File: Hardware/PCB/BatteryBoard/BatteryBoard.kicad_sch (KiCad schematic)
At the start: 59 parts, among them J1 Conn_01x07, J2 USB_C_Receptacle_USB2.0, J3 Conn_01x07, J4 Conn_01x07, J5 Thermistor, J6 Conn_01x07, J7 Power, Q1 FDS4935A, Q2 BCV62, SW1 SW_SPDT, U1 BQ25887RGER, U2 NJW4190M, U3 AZ1084C-3.3, U4 MIC29500-5.0WT

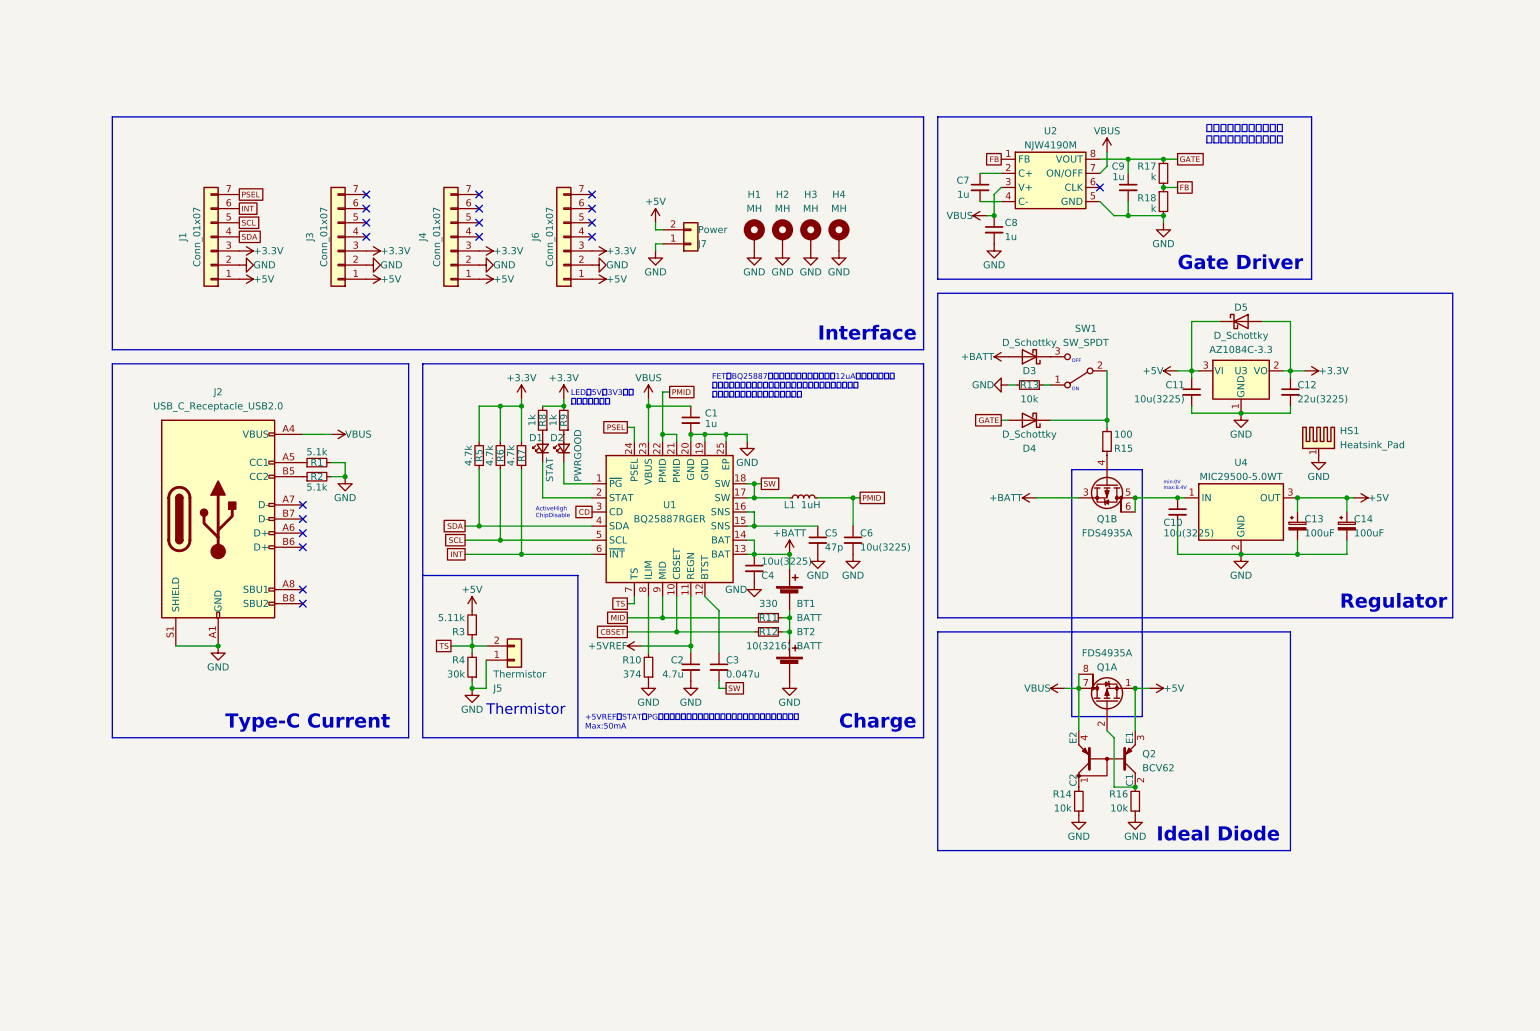
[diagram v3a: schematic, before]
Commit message: Powerpathコンを使用、部品配置
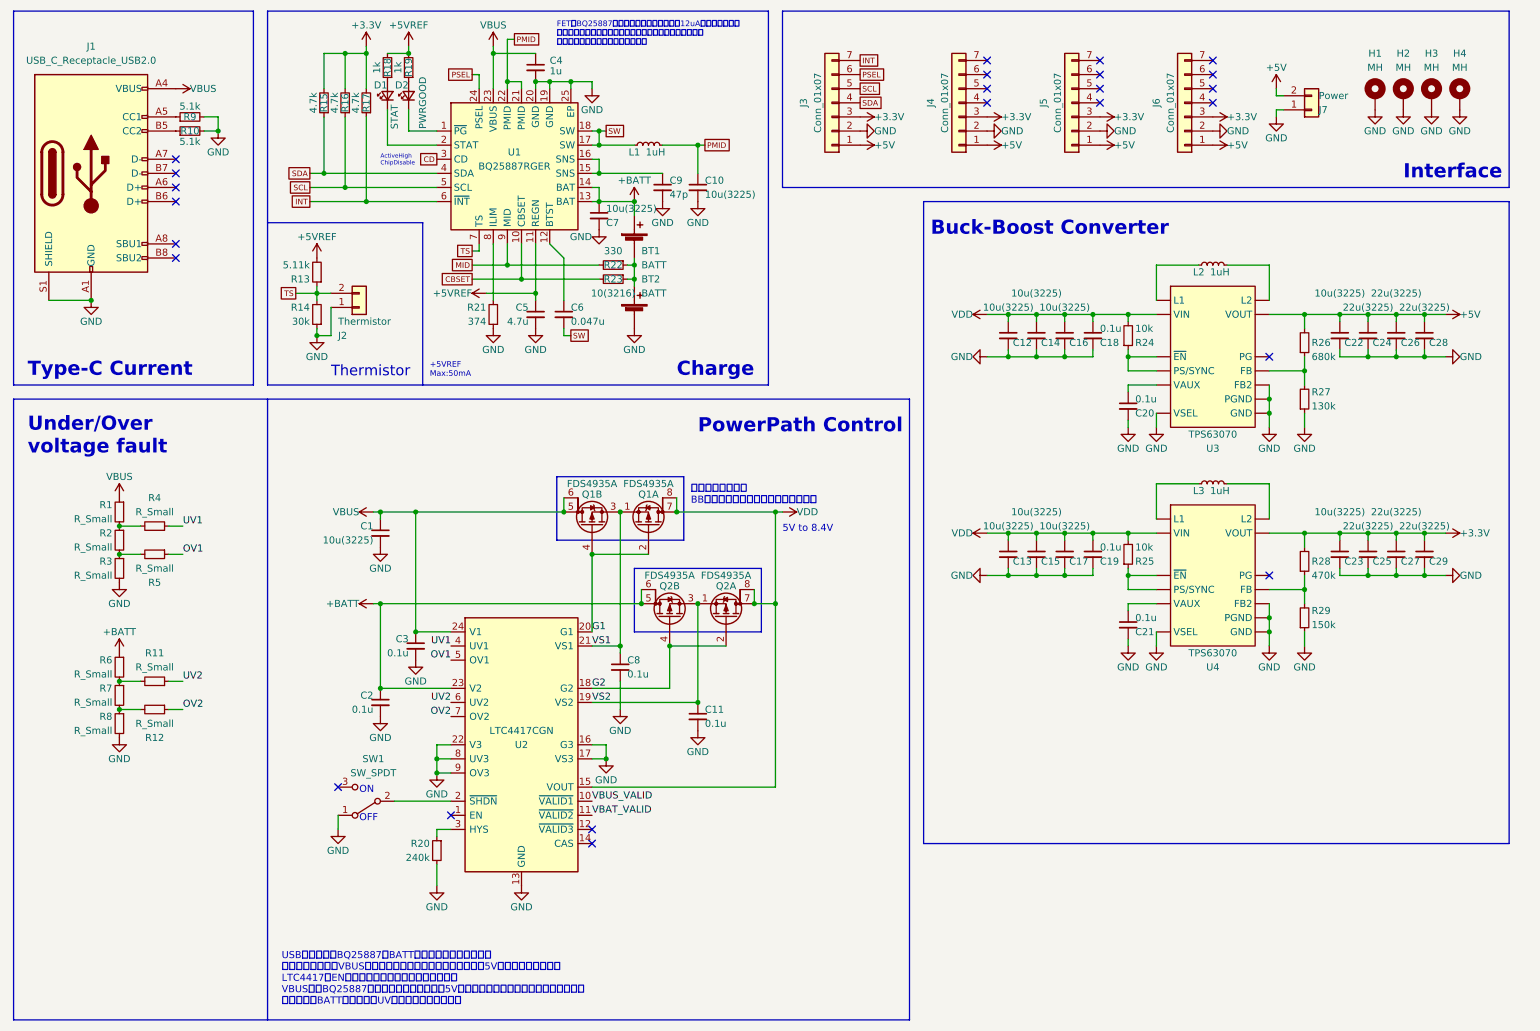
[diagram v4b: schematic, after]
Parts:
- removed C10: 10u(3225), Capacitor_SMD:C_1210_3225Metric, symbol Device:C_Small
- removed C13, C14: 100uF, Capacitor_THT:CP_Radial_D5.0mm_P2.00mm, symbol Device:C_Polarized_Small
- removed C7, C9: 1u, Capacitor_SMD:C_0603_1608Metric, symbol Device:C_Small
- removed D3, D4, D5: D_Schottky, CUHS20S30:CUHS20S30, symbol Device:D_Schottky
- removed HS1: Heatsink_Pad, Heatsink_extlib:Heatsink_15x11mm_11PB015, symbol Mechanical:Heatsink_Pad
- removed Q2: BCV62, Package_TO_SOT_SMD:SOT-143, symbol Device:Q_Dual_PNP_C2C1E1E2
- removed R13, R14, R16: 10k, Resistor_SMD:R_0603_1608Metric, symbol Device:R_Small
- removed R15: 100, Resistor_SMD:R_0603_1608Metric, symbol Device:R_Small
- removed R17, R18: k, Resistor_SMD:R_0603_1608Metric, symbol Device:R_Small
- removed U2: NJW4190M, Kicad_Akiyuki_Footprint:DMP-8_P1.27mm, symbol NJW4190M:NJW4190M
- removed U3: AZ1084C-3.3, Package_TO_SOT_SMD:TO-252-2, symbol Regulator_Linear:AZ1084-3.3
- removed U4: MIC29500-5.0WT, Package_TO_SOT_THT:TO-220-3_Vertical, symbol Regulator_Linear:LT1963AxST-3.3
- added C1, C13, C14, C15, C16, C17, C22, C23: 10u(3225), Capacitor_SMD:C_1210_3225Metric, symbol Device:C_Small
- added C18, C19, C2, C20, C21, C3: 0.1u, Capacitor_SMD:C_0603_1608Metric, symbol Device:C_Small
- added C24, C25, C26, C27, C28, C29: 22u(3225), Capacitor_SMD:C_1210_3225Metric, symbol Device:C_Small
- added L2, L3: 1uH, Inductor_SMD:L_1210_3225Metric, symbol Device:L_Small
- added Q2: FDS4935A, Package_SO:SOIC-8_3.9x4.9mm_P1.27mm, symbol Device:Q_Dual_PMOS_S1G1S2G2D2D2D1D1
- added R1, R11, R12, R2, R3, R4, R5, R6, R7, R8: R_Small, Resistor_SMD:R_0603_1608Metric, symbol Device:R_Small
- added R20: 240k, Resistor_SMD:R_0603_1608Metric, symbol Device:R_Small
- added R24, R25: 10k, Resistor_SMD:R_0603_1608Metric, symbol Device:R_Small
- added R26: 680k, Resistor_SMD:R_0603_1608Metric, symbol Device:R_Small
- added R27: 130k, Resistor_SMD:R_0603_1608Metric, symbol Device:R_Small
- added R28: 470k, Resistor_SMD:R_0603_1608Metric, symbol Device:R_Small
- added R29: 150k, Resistor_SMD:R_0603_1608Metric, symbol Device:R_Small
- added U2: LTC4417CGN, Package_SO:SSOP-24_3.9x8.7mm_P0.635mm, symbol Power_Management:LTC4417CGN
- added U3, U4: TPS63070, Module_SparkFun_Buck-Boost:VQFN-15-HR(3X2.5), symbol Module_SparkFun_Buck-Boost:TPS63070
- C11: value 10u(3225) -> 0.1u; footprint Capacitor_SMD:C_1210_3225Metric -> Capacitor_SMD:C_0603_1608Metric
- C12: value 22u(3225) -> 10u(3225)
- C8: value 1u -> 0.1u
- renumbered C6 to C10, C1 to C4, C2 to C5, C3 to C6, C4 to C7, C5 to C9, J2 to J1, J5 to J2, J1 to J3, J3 to J4, J4 to J5, R2 to R10, R3 to R13, R4 to R14, R5 to R15, R6 to R16, R7 to R17, R8 to R18, R9 to R19, R10 to R21, R11 to R22, R12 to R23, R1 to R9
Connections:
- net +3.3V: now also C23.1, C25.1, C27.1, C29.1, R28.2, U4.P$7/8 (VOUT); no longer C12.1, R18.2, R19.2
- net +5V: now also C22.1, C24.1, C26.1, C28.1, R26.2, U3.P$7/8 (VOUT); no longer C11.1, Q1.1 (S), R13.2
- net +5VREF: now also R13.2, R18.2, R19.2
- net +BATT: now also C2.1, Q2.5 (D), Q2.6 (G), R6.1, U2.23 (V2); no longer Q1.3 (S)
- net GND: now also SW1.1 (A), C1.2, C13.2, C14.2, C15.2, C16.2, C17.2, C18.2, C19.2, C2.2, C20.2, C21.2, C22.2, C23.2, C24.2, C25.2, C26.2, C27.2, C28.2, C29.2, C3.2, R20.2, R27.1, R29.1, R3.2, R8.2, U2.13 (GND), U2.16 (G3), U2.17 (VS3), U2.22 (V3), U2.8 (UV3), U2.9 (OV3), U3.P$10 (PGND), U3.P$15 (VSEL), U3.P$4 (GND), U3.P$6 (FB2), U4.P$10 (PGND), U4.P$15 (VSEL), U4.P$4 (GND), U4.P$6 (FB2)
- net INT: now also J3.7 (Pin_7); no longer J3.6 (Pin_6)
- net PSEL: now also J3.6 (Pin_6); no longer J3.7 (Pin_7)
- net VBUS: now also Q1.5 (D), Q1.6 (G), C1.1, C3.1, R1.1, U2.24 (V1); no longer C8.1, Q1.7 (D), Q1.8 (G)
- net G1: now reaches Q1.4 (G)
- net G1: now also Q1.2 (G), U2.20 (G1)
- net at SW1.2 (B): now also U2.2 (~{SHDN})
- new net: R20.1, U2.3 (HYS)
- new net: R24.1, U3.P$1 (PS/SYNC), U3.P$14 (~{EN})
- new net: R25.1, U4.P$1 (PS/SYNC), U4.P$14 (~{EN})
- new net: C20.1, U3.P$3 (VAUX)
- new net: C21.1, U4.P$3 (VAUX)
- new net: R11.2, R6.2, R7.1
- new net: L2.1, U3.P$11 (L1)
- new net: L2.2, U3.P$9 (L2)
- new net: R12.2, R7.2, R8.1
- new net: R1.2, R2.1, R4.2
- new net: R2.2, R3.1, R5.2
- new net: R26.1, R27.2, U3.P$5 (FB)
- new net: L3.1, U4.P$11 (L1)
- new net: R28.1, R29.2, U4.P$5 (FB)
- new net: L3.2, U4.P$9 (L2)
- new net G2: Q2.2 (G), Q2.4 (G), U2.18 (G2)
- new net OV1: R5.1, U2.5 (OV1)
- new net OV2: R12.1, U2.7 (OV2)
- new net UV1: R4.1, U2.4 (UV1)
- new net UV2: R11.1, U2.6 (UV2)
- new net VBAT_VALID: U2.11 (~{VALID2})
- new net VBUS_VALID: U2.10 (~{VALID1})
- new net VDD: C12.1, C13.1, C14.1, C15.1, C16.1, C17.1, C18.1, C19.1, Q1.7 (D), Q1.8 (G), Q2.7 (D), Q2.8 (G), R24.2, R25.2, U2.15 (VOUT), U3.P$12/13 (VIN), U4.P$12/13 (VIN)
- new net VS1: C8.1, Q1.1 (S), Q1.3 (S), U2.21 (VS1)
- new net VS2: C11.1, Q2.1 (S), Q2.3 (S), U2.19 (VS2)
- no-connect marks 19 -> 24
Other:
- note added: "+5VREF Max:50mA"
- note added: "5V to 8.4V"
- note added: "Buck-Boost Converter"
- note added: "PowerPath Control"
- note added: "USBが未接続でBQ25887がBATTから給電されている時に サーミスタ電源がVBUSでは使えないため、サーミスタ電源は5Vである必要がある。 LTC4417のENにスイッチを付けてオフにすると、 VBUSからBQ25887に給電、充電されるけど5Vサーミスタが使えないことになるので、 スイッチはBATT側につけてUVフォルトを作成する。"
- note added: "Under/Over voltage fault"
- note added: "出力コンデンサは BBコンバータの入力コンデンサと共有"
- note removed: "+5VREFはSTATとPGのプルアップとサーミスタに使えるが、敢えて使わない Max:50mA"
- note removed: "Gate Driver"
- note removed: "Ideal Diode"
- note removed: "LEDが5Vか3V3かは 配線して決める"
- note removed: "Regulator"
- note removed: "min:0V max:8.4V"
- note removed: "フィードバック用抵抗は プルダウン抵抗を兼ねる"
- moved on the sheet: BT1, BT2, C10, C4, C5, C6, C7, C9, D1, D2, H1, H2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
